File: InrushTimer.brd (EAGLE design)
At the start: 62.2 x 41.3 mm, 71 parts, among them IC2 TLC272D, IC3 4076N, IC6 555, Q2 TIP41C

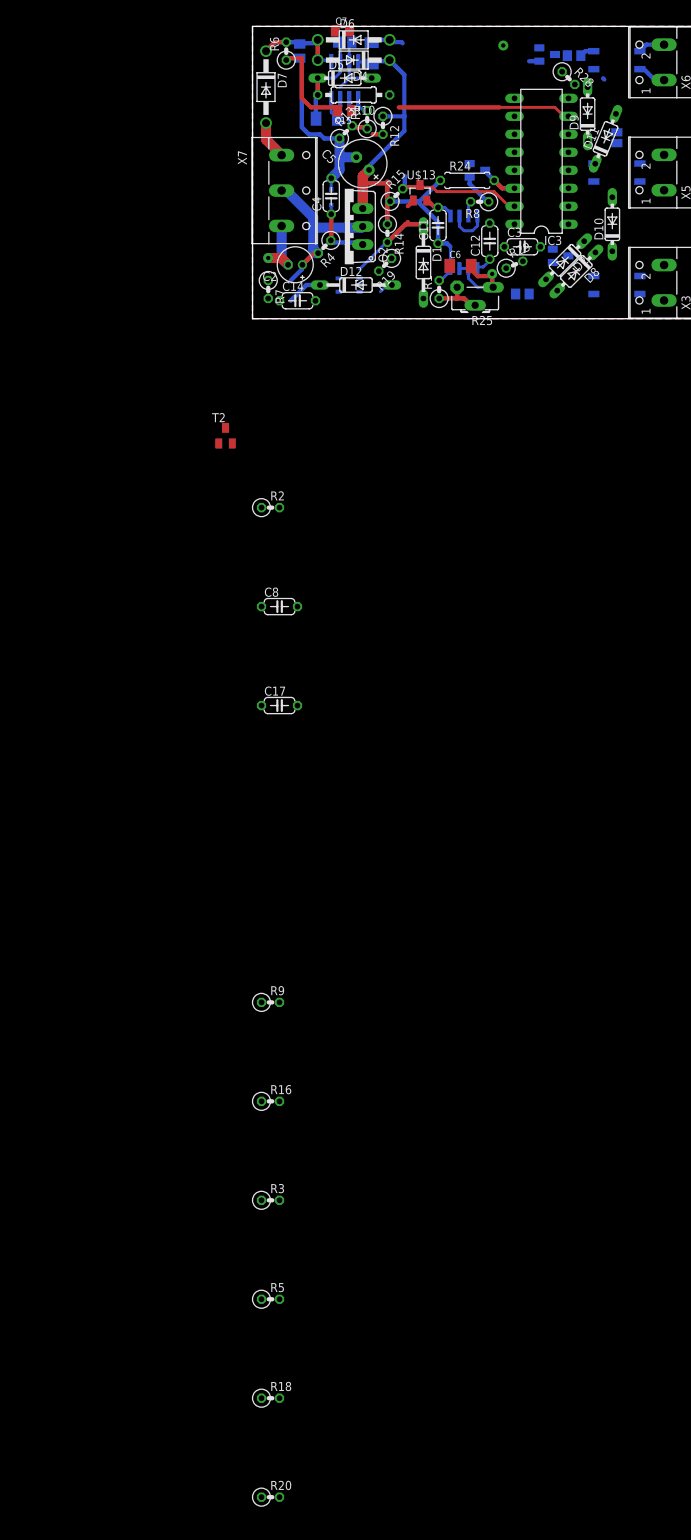
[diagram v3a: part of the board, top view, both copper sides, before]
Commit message: Updated optotriac symbol
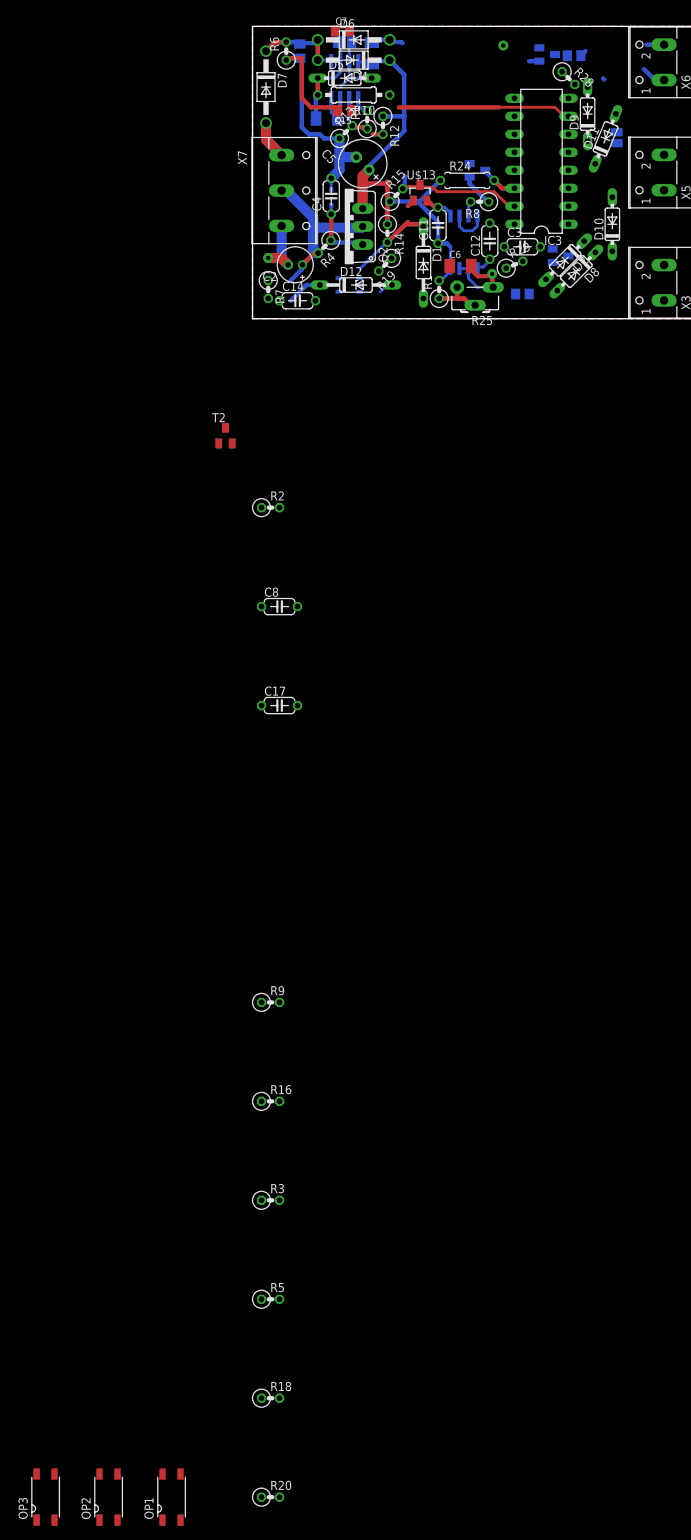
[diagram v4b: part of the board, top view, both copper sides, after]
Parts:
- removed U$5, U$8, U$9: FODM3053, SHoleLib:FODM
- added OP1, OP2, OP3: FODM3053, SHoleLib:FODM
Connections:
- net N$10: now also OP3.4; no longer U$5.4
- net N$12: now also OP1.3; no longer U$8.3
- net N$15: now also OP1.1; no longer U$8.1
- net N$17: now also OP2.2; no longer U$9.2
- net N$18: now also OP3.2; no longer U$5.2
- net N$20: now also OP2.4; no longer U$9.4
- net N$21: now also OP2.3; no longer U$9.3
- net N$4: now also OP1.4; no longer U$8.4
- net N$5: now also OP3.3; no longer U$5.3
- net N$6: now also OP1.2; no longer U$8.2
- net V12: now also OP2.1, OP3.1; no longer U$5.1, U$9.1
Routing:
- net N$5: track 3.80 -> 2.51 mm
- net N$18: track 2.10 -> 0.90 mm
- net N$10: track 4.06 -> 3.50 mm
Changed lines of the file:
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@@
 <element name="C4" library="rcl" package="C050-024X044" value="100nF" x="11.1125" y="17.30375" rot="R90"/>
 <element name="C13" library="rcl" package="C1206K" value="100nF" x="10.4775" y="28.2575" rot="MR180"/>
-<element name="U$5" library="SHoleLib" package="FODM" value="FODM3053" x="51.435" y="36.5125" rot="MR90"/>
 <element name="Q2" library="transistor-power" package="TO220AV" value="TIP41C" x="13.0175" y="13.0175" rot="R90"/>
 <element name="R17" library="rcl" package="R0805" value="1K" x="38.1" y="3.4925" rot="MR0"/>
@@
 <element name="R24" library="rcl" package="0207/7" value="51K" x="30.32125" y="19.52625"/>
 <element name="C11" library="rcl" package="C050-024X044" value="100nF" x="26.19375" y="13.17625" rot="R90"/>
-<element name="U$8" library="SHoleLib" package="FODM" value="FODM3053" x="51.435" y="4.7625" rot="MR90"/>
 <element name="R25" library="pot" package="CA6H_MOD" value="220K" x="31.4325" y="4.445" rot="R180"/>
 <element name="X3" library="con-wago-500" package="W237-102" value="" x="56.8325" y="5.08" rot="R90">
@@
 <element name="C3" library="rcl" package="C050-024X044" value="100nF" x="38.1" y="10.16"/>
 <element name="IC6" library="linear" package="SO08-555" value="555" x="29.845" y="10.795" rot="MR180"/>
-<element name="U$9" library="SHoleLib" package="FODM" value="FODM3053" x="51.435" y="20.6375" rot="MR90"/>
 <element name="C7" library="rcl" package="C0805K" value="1nF" x="12.7" y="40.64"/>
 <element name="T2" library="transistor" package="SOT23-BEC" value="" x="-3.81" y="-16.51"/>
@@
 <element name="R18" library="rcl" package="0207/2V" value="100R" x="2.54" y="-152.4"/>
 <element name="R20" library="rcl" package="0207/2V" value="10K" x="2.54" y="-166.37"/>
+<element name="OP1" library="SHoleLib" package="FODM" value="FODM3053" x="-11.43" y="-166.37"/>
+<element name="OP2" library="SHoleLib" package="FODM" value="FODM3053" x="-20.32" y="-166.37"/>
+<element name="OP3" library="SHoleLib" package="FODM" value="FODM3053" x="-29.21" y="-166.37"/>
 </elements>
 <signals>
@@
 <contactref element="R28" pad="1"/>
 <contactref element="C3" pad="1"/>
-<contactref element="U$5" pad="1"/>
 <contactref element="R29" pad="1"/>
 <contactref element="IC6" pad="8"/>
@@
 <wire x1="26.19375" y1="13.6525" x2="26.19375" y2="10.63625" width="0.6096" layer="16"/>
 <contactref element="IC3" pad="12"/>
-<contactref element="U$9" pad="1"/>
-<wire x1="48.185" y1="35.2425" x2="49.4938875" y2="33.933615625" width="0" layer="19" extent="16-16"/>
-<wire x1="43.710721875" y1="34.870525" x2="48.185" y2="35.2425" width="0" layer="19" extent="16-16"/>
-<wire x1="36.98875" y1="23.495" x2="43.710721875" y2="34.870525" width="0" layer="19" extent="1-1"/>
-<wire x1="36.98875" y1="13.335" x2="36.98875" y2="23.495" width="0" layer="19" extent="1-1"/>
-<wire x1="35.56" y1="10.16" x2="36.98875" y2="13.335" width="0" layer="19" extent="1-1"/>
+<contactref element="OP2" pad="1"/>
+<contactref element="OP3" pad="1"/>
+<wire x1="-21.59" y1="-169.62" x2="-30.48" y2="-169.62" width="0" layer="19" extent="1-1"/>
+<wire x1="26.3525" y1="5.3975" x2="-21.59" y2="-169.62" width="0" layer="19" extent="1-1"/>
+<wire x1="19.1008" y1="19.1008" x2="19.05" y2="19.372171875" width="0" layer="19" extent="1-16"/>
+<wire x1="35.56" y1="10.16" x2="27.94" y2="10.16" width="0" layer="19" extent="16-16"/>
 <wire x1="35.815421875" y1="7.133990625" x2="35.56" y2="10.16" width="0" layer="19" extent="1-1"/>
-<wire x1="27.94" y1="10.16" x2="35.56" y2="10.16" width="0" layer="19" extent="16-16"/>
-<wire x1="19.1008" y1="19.1008" x2="19.05" y2="19.372171875" width="0" layer="19" extent="1-16"/>
-<wire x1="48.185" y1="19.3675" x2="36.98875" y2="23.495" width="0" layer="19" extent="16-16"/>
+<wire x1="36.98875" y1="13.335" x2="35.56" y2="10.16" width="0" layer="19" extent="1-1"/>
+<wire x1="36.98875" y1="23.495" x2="36.98875" y2="13.335" width="0" layer="19" extent="1-1"/>
+<wire x1="43.710721875" y1="34.870525" x2="36.98875" y2="23.495" width="0" layer="19" extent="1-1"/>
+<wire x1="49.4938875" y1="33.933615625" x2="43.710721875" y2="34.870525" width="0" layer="19" extent="16-16"/>
 </signal>
 <signal name="ZERO">
@@
 <contactref element="U$3" pad="3"/>
 <contactref element="D10" pad="C"/>
-<contactref element="U$8" pad="2"/>
-<wire x1="48.185" y1="6.0325" x2="50.8" y2="9.525" width="0" layer="19" extent="16-16"/>
-<wire x1="44.5975" y1="8.89" x2="48.185" y2="6.0325" width="0" layer="19" extent="16-16"/>
+<contactref element="OP1" pad="2"/>
+<wire x1="44.5975" y1="8.89" x2="-10.16" y2="-169.62" width="0" layer="19" extent="1-16"/>
+<wire x1="50.8" y1="9.525" x2="44.5975" y2="8.89" width="0" layer="19" extent="16-16"/>
 </signal>
 <signal name="N$22">
@@
 <signal name="N$5">
 <contactref element="X6" pad="2"/>
-<contactref element="U$5" pad="3"/>
-<wire x1="54.685" y1="37.7825" x2="55.5975" y2="38.695" width="0.6096" layer="16"/>
 <wire x1="55.5975" y1="38.695" x2="58.1025" y2="38.695" width="0.6096" layer="16"/>
+<contactref element="OP3" pad="3"/>
+<wire x1="55.5975" y1="38.695" x2="-27.94" y2="-163.12" width="0" layer="19" extent="1-16"/>
 </signal>
 <signal name="N$10">
 <contactref element="X6" pad="1"/>
-<contactref element="U$5" pad="4"/>
 <wire x1="58.1025" y1="33.695" x2="56.7925" y2="33.695" width="0.6096" layer="16"/>
 <wire x1="56.7925" y1="33.695" x2="55.245" y2="35.2425" width="0.6096" layer="16"/>
-<wire x1="55.245" y1="35.2425" x2="54.685" y2="35.2425" width="0.6096" layer="16"/>
+<contactref element="OP3" pad="4"/>
+<wire x1="56.7925" y1="33.695" x2="-30.48" y2="-163.12" width="0" layer="19" extent="1-16"/>
 </signal>
 <signal name="N$18">
-<contactref element="U$5" pad="2"/>
 <contactref element="R26" pad="1"/>
-<wire x1="48.185" y1="37.7825" x2="46.9875" y2="37.7825" width="0.6096" layer="16"/>
 <wire x1="46.9875" y1="37.7825" x2="46.3525" y2="37.1475" width="0.6096" layer="16"/>
+<contactref element="OP3" pad="2"/>
+<wire x1="46.3525" y1="37.1475" x2="-27.94" y2="-169.62" width="0" layer="19" extent="1-16"/>
 </signal>
 <signal name="DISABLE_A">
@@
 <signal name="N$4">
 <contactref element="X3" pad="1"/>
-<contactref element="U$8" pad="4"/>
-<wire x1="54.685" y1="3.4925" x2="58.1025" y2="2.58" width="0" layer="19" extent="16-16"/>
+<contactref element="OP1" pad="4"/>
+<wire x1="58.1025" y1="2.58" x2="-12.7" y2="-163.12" width="0" layer="19" extent="1-1"/>
 </signal>
 <signal name="N$12">
 <contactref element="X3" pad="2"/>
-<contactref element="U$8" pad="3"/>
-<wire x1="54.685" y1="6.0325" x2="58.1025" y2="7.58" width="0" layer="19" extent="16-16"/>
+<contactref element="OP1" pad="3"/>
+<wire x1="58.1025" y1="7.58" x2="-10.16" y2="-163.12" width="0" layer="19" extent="1-1"/>
 </signal>
 <signal name="N$15">
-<contactref element="U$8" pad="1"/>
 <contactref element="R17" pad="2"/>
-<wire x1="37.15" y1="3.4925" x2="48.185" y2="3.4925" width="0" layer="19" extent="16-16"/>
+<contactref element="OP1" pad="1"/>
+<wire x1="37.15" y1="3.4925" x2="-12.7" y2="-169.62" width="0" layer="19" extent="1-16"/>
 </signal>
 <signal name="N$17">
-<contactref element="U$9" pad="2"/>
 <contactref element="R17" pad="1"/>
-<wire x1="39.05" y1="3.4925" x2="48.185" y2="21.9075" width="0" layer="19" extent="16-16"/>
+<contactref element="OP2" pad="2"/>
+<wire x1="39.05" y1="3.4925" x2="-19.05" y2="-169.62" width="0" layer="19" extent="1-16"/>
 </signal>
 <signal name="N$20">
-<contactref element="U$9" pad="4"/>
 <contactref element="X5" pad="2"/>
-<wire x1="54.685" y1="19.3675" x2="58.1025" y2="23.1375" width="0" layer="19" extent="16-16"/>
+<contactref element="OP2" pad="4"/>
+<wire x1="58.1025" y1="23.1375" x2="-21.59" y2="-163.12" width="0" layer="19" extent="1-1"/>
 </signal>
 <signal name="N$21">
-<contactref element="U$9" pad="3"/>
 <contactref element="X5" pad="1"/>
-<wire x1="58.1025" y1="18.1375" x2="54.685" y2="21.9075" width="0" layer="19" extent="16-16"/>
+<contactref element="OP2" pad="3"/>
+<wire x1="58.1025" y1="18.1375" x2="-19.05" y2="-163.12" width="0" layer="19" extent="1-1"/>
 </signal>
 <signal name="N$13">

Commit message: Fixed missing libraries by moving parts into local lib. Renumbered components.
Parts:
- removed IC6: 555, linear:SO08-555
- removed R26: 1K, rcl:R0805
- removed U$13, U$3, U$6, U$7: 2N7002, transistor-fet:SOT23
- removed U$4: BU48XXG, ROHM_By_element14_Batch_1:SOT95P280X125-5N
- removed X5: (no value), con-wago-500:W237-102
- added IC1: TLC272D, linear:SO08
- added Q1: TIP41C, transistor-power:TO220AV
- added Q3, Q4, Q5: TRANSISTOR-FET_2N7002, InrushTimer:TRANSISTOR-FET_SOT23
- added R21: 10K, rcl:0207/2V
- added U1: ROHM_BY_ELEMENT14_BATCH_1_BU48XXG, InrushTimer:ROHM_BY_ELEMENT14_BATCH_1_SOT95P280X125-5N
- added X4: (no value), con-wago-500:W237-102
- C1: value 100nF -> 10uF; device rcl:C1206K -> rcl:E2-5
- C10: value 1nF -> 10pF (DNF)
- C11, C4: value 100nF -> 10nF
- C12, C14: value 10nF -> 100nF
- C13: value 100nF -> 2.2uF
- C15: value 10pF (DNF) -> 100nF (DNF); device rcl:C0805K -> rcl:C050-024X044
- C2: value 10uF -> 100nF; device rcl:E2-5 -> rcl:C050-024X044
- C3: value 100nF -> 100uF; device rcl:C050-024X044 -> rcl:E2,5-7
- C5: value 100uF -> 10nF; device rcl:E2,5-7 -> rcl:C0805K
- C6: value 2.2uF -> 1nF; device rcl:C1206K -> rcl:C0805K
- C8: value 100nF (DNF) -> 100nF; device rcl:C050-024X044 -> rcl:C1206K
- C9: value 10nF -> 100nF; device rcl:C0805K -> rcl:C1206K
- D1: value BZX55 -> Z12V; device diode:DO35Z10 -> diode:SOD323-R
- D12: value BZX55 -> 1N4148DO35-7; device diode:DO35Z10 -> diode:DO35-7
- D2: value 1N4148DO35-7 -> BZX55; device diode:DO35-7 -> diode:DO35Z10
- D3: value Z12V -> BZX55; device diode:SOD323-R -> diode:DO35Z10
- D4: value 1n4001 -> STTH110
- D5: value 1N4148DO35-7 -> 1n4001; device diode:DO35-7 -> diode:DO41-10
- D7: value STTH110 -> 1N4148DO35-7; device diode:DO41-10 -> diode:DO35-7
- IC2: value TLC272D -> 555; device linear:SO08 -> linear:SO08-555
- Q2: value TIP41C -> TRANSISTOR-FET_2N7002; device transistor-power:TO220AV -> InrushTimer:TRANSISTOR-FET_SOT23
- R1: value 100K -> 4K7
- R10: value 9.1M -> 10K; device rcl:0207/10 -> rcl:0207/2V
- R12: value 200K -> 100K
- R13: value 100K -> 200K
- R14: value 22K -> 100K
- R15: value 51K -> 220K; device rcl:0207/2V -> pot:CA6H_MOD
- R16: value 10K -> 1K
- R17: value 1K -> 51K; device rcl:R0805 -> rcl:0207/7
- R18: value 100R -> 10K
- R2: value 10K -> 27K
- R24: value 51K -> 1K; device rcl:0207/7 -> rcl:R0805
- R25: value 220K -> 1K; device pot:CA6H_MOD -> rcl:R0805
- R4: value 4K7 -> 10K
- R5: value 10K -> 100R
- R7: value 27K -> 51K
- R8: value 1K -> 22K
- R9: value 10K -> 9.1M; device rcl:0207/2V -> rcl:0207/10
- moved R10 198.3 mm to (2.54, -166.4), turned to 0 degrees
- moved Q2 195.7 mm to (-30.5, -177.8), turned to 0 degrees
- moved R3 133.1 mm to (18.7, 7.62), turned to 225 degrees
- moved R16 130.4 mm to (32.1, 16.5), turned to 180 degrees
- moved R9 128.6 mm to (14.3, 31.6), turned to 180 degrees
- moved R19 119.2 mm to (2.54, -110.5), turned to 0 degrees
- moved C8 79.2 mm to (16.8, 37.5), flipped to the bottom, turned to 90 degrees
- moved C15 70.6 mm to (3.81, -40.6), turned to 0 degrees
- moved R4 37.6 mm to (2.54, -26.7), turned to 0 degrees
- moved D12 37.2 mm to (50.8, 13.3), turned to 90 degrees
- moved C6 35.6 mm to (13.0, 39.1), flipped to the bottom, turned to 180 degrees
- moved R8 34.6 mm to (4.76, 37.8), turned to 90 degrees
- moved C14 32.7 mm to (38.1, 10.2)
- moved C1 31.7 mm to (6.03, 7.62), flipped to the top, turned to 180 degrees
- moved R2 30.8 mm to (2.22, 4.13), turned to 270 degrees
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- renumbered C17 to C16, R28 to R22, R29 to R23, SJ2 to SJ1, T2 to T1, X6 to X2, X7 to X1
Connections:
- net DISABLE_A: now also D12.A; no longer D10.A
- net HYST: now also IC1.2, R11.2; no longer IC2.2, R13.2
- net N$1: now also D4.A; no longer D7.A
- net N$10: now also OP1.4; no longer OP3.4
- net N$11: now also C5.2, D4.C, D5.A, IC1.5, R8.2; no longer C9.2, D4.A, D7.C, IC2.5, R6.2
- net N$12: now also OP3.3, X4.2; no longer OP1.3, X3.2
- net N$13: now also R4.2, U1.2; no longer R2.2, U$4.2
- net N$14: now also C4.1, D2.C, R2.2, R3.2; no longer C14.1, D12.C, R19.2, R7.2
- net N$15: now also OP3.1, R25.2; no longer OP1.1, R17.2
- net N$16: now also D9.C, R18.1; no longer D2.C, R3.1
- net N$17: now also R25.1; no longer R17.1
- net N$18: now also OP1.2, R24.1; no longer OP3.2, R26.1
- net N$19: now also R20.2; no longer R5.2
- net N$2: now also R14.1, R15.E, R15.S; no longer R1.1, R25.E, R25.S
- net N$20: now also X3.2; no longer X5.2
- net N$21: now also X3.1; no longer X5.1
- net N$22: now also D8.C, R20.1; no longer D11.C, R5.1
- net N$23: now also R5.2, U1.1; no longer R18.2, U$4.1
- net N$24: now also D11.C, R21.1; no longer D9.C, R9.1
- net N$25: now also R19.2; no longer R16.2
- net N$26: now also IC1.3, R10.2, R13.1; no longer IC2.3, R11.1, R20.2
- net N$28: now also C13.2, IC2.6, IC2.7, R15.A; no longer C6.2, IC6.6, IC6.7, R25.A
- net N$3: now also R21.2; no longer R9.2
- net N$30: now also D10.C, R19.1; no longer D8.C, R16.1
- net N$31: now also Q4.3, R24.2; no longer R26.2, U$6.3
- net N$32: now also R18.2; no longer R3.2
- net N$36: now also Q3.1, R16.1; no longer R8.1, U$7.1
- net N$4: now also OP3.4, X4.1; no longer OP1.4, X3.1
- net N$40: now also C11.1, IC2.5; no longer C12.1, IC6.5
- net N$48: now also IC2.3, R16.2; no longer IC6.3, R8.2
- net N$5: now also OP1.3; no longer OP3.3
- net N$6: now also D12.C, OP3.2, Q5.3; no longer D10.C, OP1.2, U$3.3
- net N$7: now also C6.2, D7.A, IC1.7, R10.1; no longer C10.2, D5.A, IC2.7, R20.1
- net N$8: now also C2.1, D1.C, Q1.B, R1.1; no longer C4.1, D3.C, Q2.B, R4.1
- net N$9: now also C6.1, C9.1, D7.C, IC1.6, R9.2; no longer C10.1, C13.1, D5.C, IC2.6, R10.2
- net ON_A_SYNC: now also C15.2, D8.A, Q4.1; no longer C8.2, D9.A, U$6.1
- net ON_B: now also Q3.3, R17.2; no longer R24.2, U$7.3
- net ON_B_SYNC: now also D10.A, D9.A, Q5.1; no longer D2.A, D8.A, U$3.1
- net PEAK: now also C10.1, IC1.1, R13.2; no longer C15.1, IC2.1, R11.2
- net RECT: now also C1.+, Q1.C, R1.2, R2.1; no longer C2.+, Q2.C, R4.2, R7.1
- net RESET: now also Q2.3, R7.2; no longer R15.2, U$13.3
- net RESET_N: now also D3.C, IC2.2, IC2.4, Q2.1, R5.1, R6.2; no longer D1.C, IC6.2, IC6.4, R14.2, R18.1, U$13.1
- net V12: now also C12.1, C14.1, C3.+, C8.1, D5.C, IC1.8, OP1.1, Q1.E, R11.1, R14.2, R17.1, R6.1, R7.1; no longer C1.1, C11.1, C3.1, C5.+, D4.C, IC6.8, OP3.1, Q2.E, R1.2, R12.1, R14.1, R15.1, R24.1
- net ZERO: now also C1.-, C10.2, C13.1, C15.1, C2.2, C3.-, C5.1, C8.2, C9.2, D2.A, IC1.4, IC2.1, Q2.2, Q3.2, Q4.2, Q5.2, R12.1, R3.1, R4.1, R8.1, R9.1, U1.3; no longer C1.2, C13.2, C15.2, C2.-, C3.2, C5.-, C6.1, C8.1, C9.1, D12.A, IC2.4, IC6.1, R10.1, R13.1, R19.1, R2.1, R6.1, U$13.2, U$3.2, U$4.3, U$6.2, U$7.2
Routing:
- net ON_A_SYNC: track 1.44 -> 0.00 mm
- net RESET_N: track 25.6 -> 24.5 mm
- net N$36: track 4.70 -> 3.73 mm

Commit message: Updated component packages
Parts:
- C15, C16: device rcl:C050-024X044 -> rcl:C1206K
- R10, R18, R19, R20, R21, R4: device rcl:0207/2V -> rcl:R0805
- R16: device rcl:0207/2V -> rcl:R0402
- R24, R25: device rcl:R0805 -> rcl:0207/7
- moved C15 178.6 mm to (-30.5, -215.9)
- moved C16 157.4 mm to (-30.5, -208.3)
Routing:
- net N$18: track 0.90 -> 2.31 mm
- net N$48: track 2.15 -> 2.69 mm

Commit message: Updated zener model and added annotation on schematic.
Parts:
- D1: value Z12V -> MM3Z12VT1G (12V)
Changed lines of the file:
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@@
 </autorouter>
 <elements>
-<element name="D1" library="diode" package="SOD323-R" value="Z12V" x="11.1125" y="17.145" rot="MR90"/>
+<element name="D1" library="diode" package="SOD323-R" value="MM3Z12VT1G (12V)" x="11.1125" y="17.145" rot="MR90"/>
 <element name="C1" library="rcl" package="E2-5" value="10uF" x="6.0325" y="7.62" rot="R180"/>
 <element name="C3" library="rcl" package="E2,5-7" value="100uF" x="15.5575" y="21.9075" rot="R135"/>

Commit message: Re-layed out peak detector, supply and reset generator.
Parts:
- removed D7: 1N4148DO35-7, diode:DO35-7
- removed Q1: TIP41C, transistor-power:TO220AV
- added D13: BZX55C5V6, diode:DO34Z7
- added Q6: DIODES_ZTX451DIODES_ZTX451_0_0, Diodes - ZTX451:DIODES_ZTX451_0
- C8: device rcl:C1206K -> rcl:C0805
- D2: value BZX55 -> BZX55C5V6; device diode:DO35Z10 -> diode:DO34Z7
- D3: value BZX55 -> 5082-2800; device diode:DO35Z10 -> diode:DO34-7
- D4: device diode:DO41-10 -> diode:DO41-7.6
- D5, D6: device diode:DO41-10 -> diode:DO41-10V
- R10: device rcl:R0805 -> rcl:0207/10
- R2, R5, R7: device rcl:0207/2V -> rcl:0207/7
- R9: device rcl:0207/10 -> rcl:0204/7
- T1: value (none) -> MMBTA05
- moved C15 267.7 mm to (97.8, 19.1), turned to 90 degrees
- moved Q5 258.4 mm to (82.5, 31.8), turned to 90 degrees
- moved C16 257.4 mm to (90.2, 19.1), turned to 90 degrees
- moved Q4 252.8 mm to (80.0, 34.3), turned to 90 degrees
- moved OP3 225.0 mm to (95.2, 31.8), turned to 90 degrees
- moved OP2 221.1 mm to (94.0, 22.9), turned to 90 degrees
- moved Q3 217.2 mm to (44.5, 18.4), flipped to the bottom, turned to 90 degrees
- moved OP1 215.3 mm to (94.0, 10.2), turned to 90 degrees
- moved Q2 194.4 mm to (34.6, 5.40), flipped to the bottom, turned to 135 degrees
- moved R10 192.3 mm to (11.7, 25.7), turned to 90 degrees
- moved R20 184.3 mm to (59.7, 36.8), turned to 90 degrees
- moved R18 167.0 mm to (45.7, 36.8), turned to 90 degrees
- moved R19 158.3 mm to (83.8, 25.4), turned to 90 degrees
- moved R5 155.1 mm to (17.9, 1.91), turned to 180 degrees
- moved R21 135.4 mm to (55.9, 27.9), turned to 90 degrees
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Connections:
- removed net HYST: IC1.2, R11.2, R12.2
- new net THRESH: IC1.2, R11.1, R12.1
- net N$14: now also D13.C, R2.1; no longer D2.C, R2.2
- net N$26: now also R10.1, R13.2; no longer R10.2, R13.1
- net N$7: now also D3.A, R10.2; no longer D7.A, R10.1
- net N$8: now also Q6.2, R1.2; no longer Q1.B, R1.1
- net N$9: now also D3.C; no longer D7.C
- net PEAK: now also R13.1; no longer R13.2
- net RECT: now also Q6.3, R1.1, R2.2; no longer Q1.C, R1.2, R2.1
- net RESET_N: now also D2.C; no longer D3.C
- net V12: now also Q6.1, R11.2; no longer Q1.E, R11.1
- net ZERO: now also D13.A, R12.2; no longer D3.A, R12.1
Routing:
- net V12: track 81.2 -> 24.3 mm
- net PEAK: track 27.2 -> 3.75 mm
- net RESET: track 19.2 -> 0.00 mm
- net RESET_N: track 24.5 -> 7.89 mm
- net N$28: track 14.6 -> 0.00 mm, vias 1 -> 0
- net N$2: track 14.1 -> 0.00 mm
- net HYST: track 11.9 -> 0.00 mm
- net ZERO: track 67.3 -> 77.9 mm, vias 2 -> 1
- net THRESH: track 0.00 -> 9.22 mm
- net ON_B: track 8.45 -> 0.00 mm
- net N$14: track 5.11 -> 11.0 mm
- net N$1: track 10.9 -> 5.43 mm
- net N$13: track 0.00 -> 4.50 mm
- net N$36: track 4.04 -> 0.00 mm
- net N$26: track 0.00 -> 3.75 mm
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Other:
- board size 62.2 x 41.3 mm -> 62.2 x 36 mm
